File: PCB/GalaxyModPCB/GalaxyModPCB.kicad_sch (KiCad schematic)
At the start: 57 parts, among them J1 LED RGBW Connector, J2 USB to UART, J3 Motor Connector, J4 Projector Connector, J6 Power Header, J7 Boot mode, Q1 IRLML0030, Q2 IRLML0030, Q3 IRLML0030, Q4 IRLML0030, Q5 IRLML0030, Q6 IRLML0030, SW1 On/Off, SW2 Colour, SW3 Brightness, SW4 Motor, U1 ESP32-WROOM-32, U2 AMS1117-3.3

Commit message: Part separation for reconfiguration
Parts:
- J1: footprint Connector_JST:JST_PH_B5B-PH-K_1x05_P2.00mm_Vertical -> Connector_PinHeader_1.00mm:PinHeader_1x05_P1.00mm_Vertical
- J2: footprint Connector_JST:JST_PH_B3B-PH-K_1x03_P2.00mm_Vertical -> Connector_PinHeader_1.00mm:PinHeader_1x03_P1.00mm_Vertical
- J3, J4, J6, J7: footprint Connector_JST:JST_PH_B2B-PH-K_1x02_P2.00mm_Vertical -> Connector_PinHeader_1.00mm:PinHeader_1x02_P1.00mm_Vertical

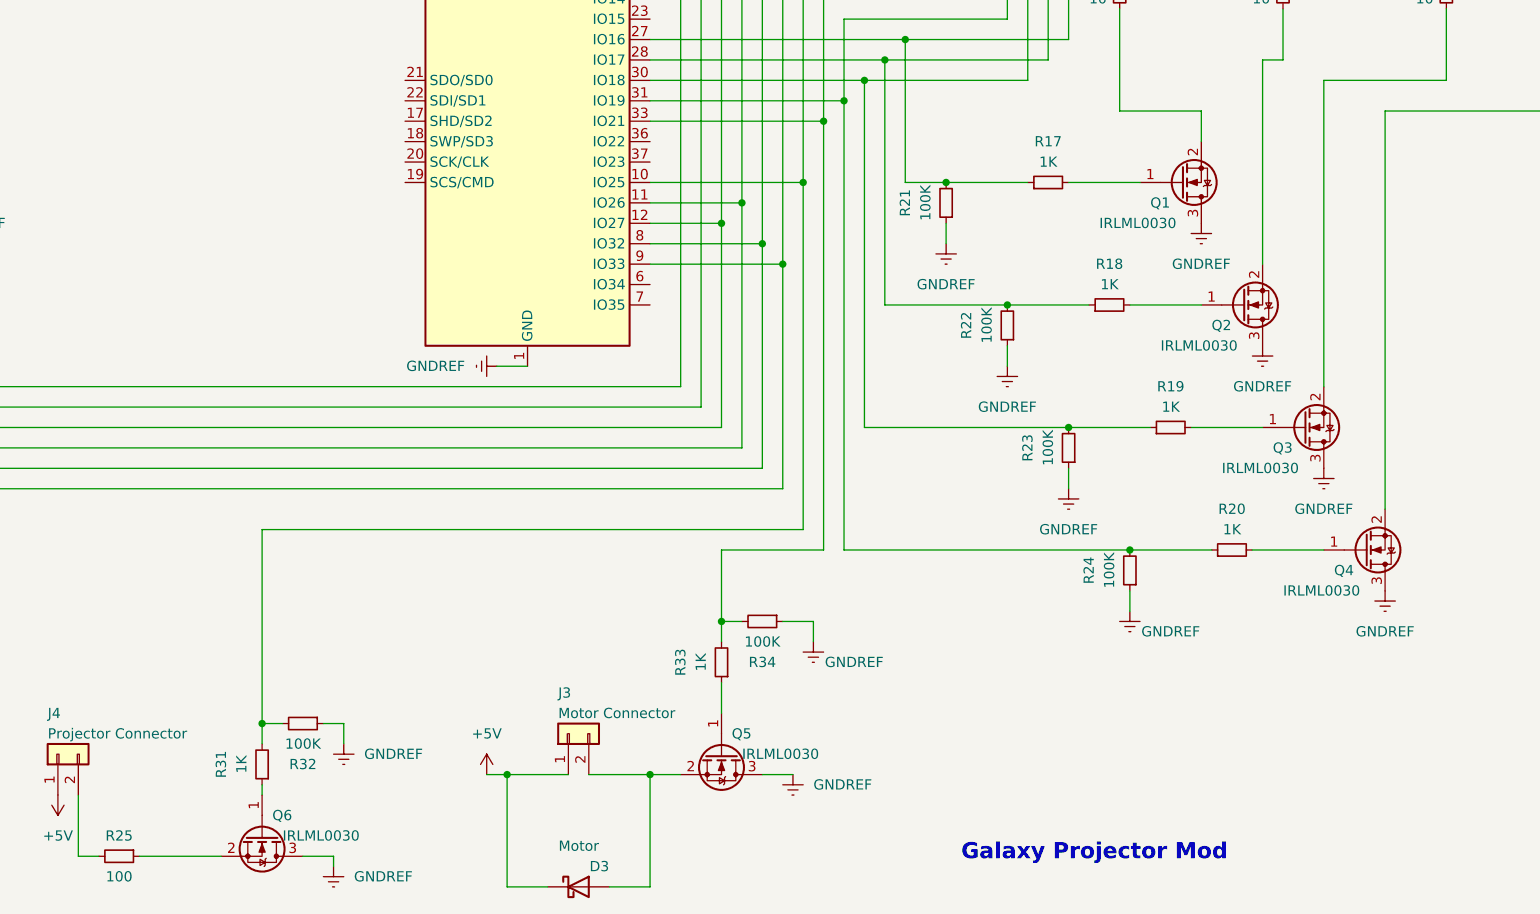
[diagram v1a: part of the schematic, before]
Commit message: Fixed transistor direction
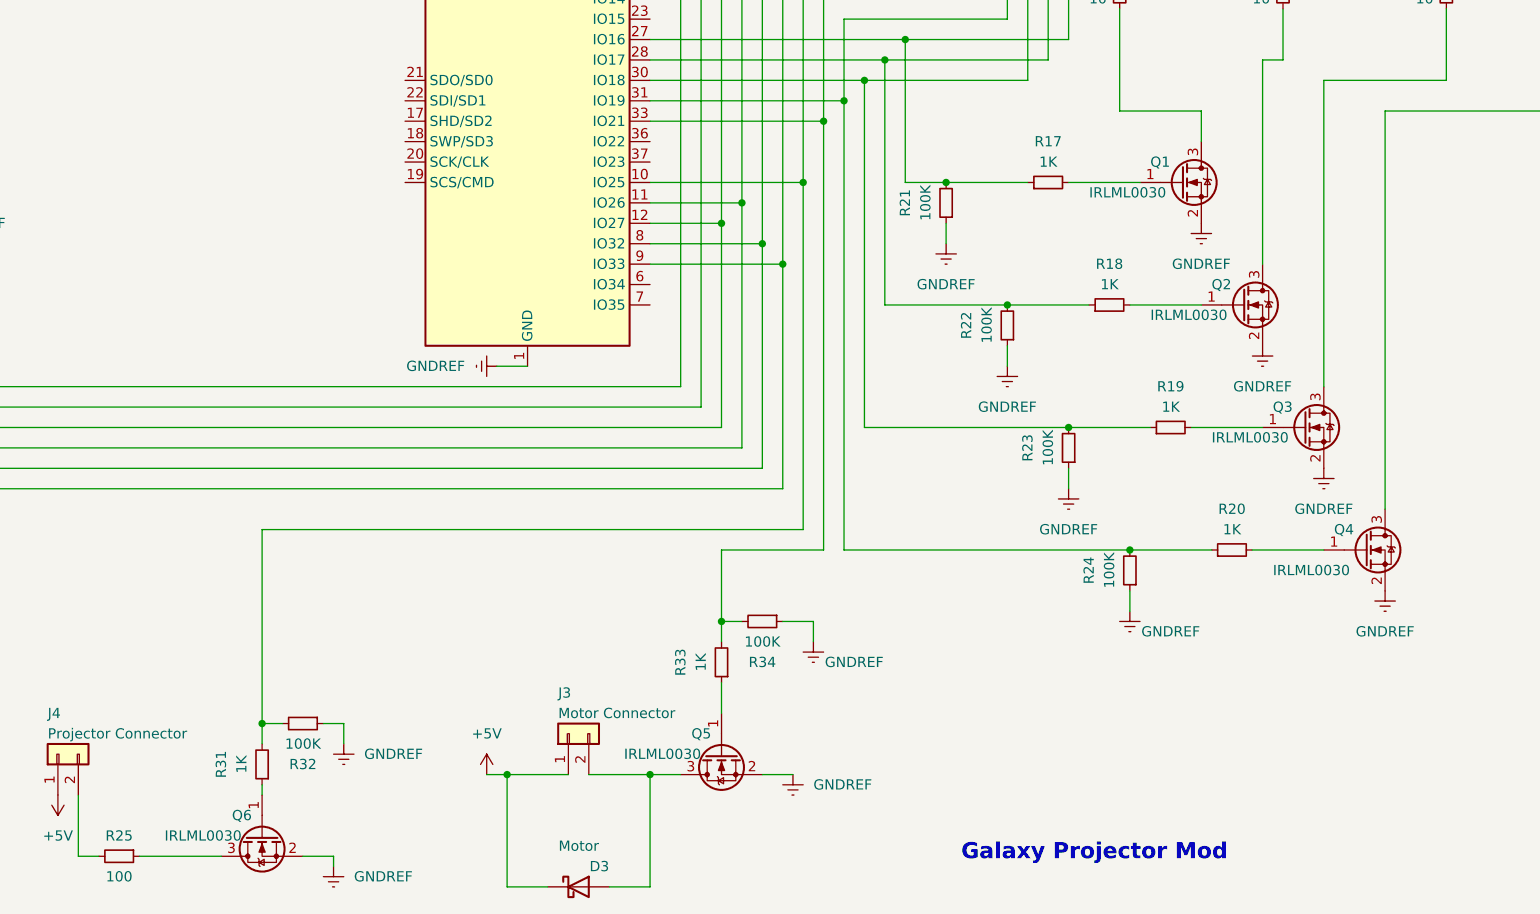
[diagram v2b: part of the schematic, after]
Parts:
- H1: footprint (none) -> MountingHole:MountingHole_2mm
- H3: footprint (none) -> MountingHole:MountingHole_2.5mm
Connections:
- net GNDREF: now also Q1.2 (S), Q2.2 (S), Q3.2 (S), Q4.2 (S), Q5.2 (S), Q6.2 (S); no longer Q1.3 (D), Q2.3 (D), Q3.3 (D), Q4.3 (D), Q5.3 (D), Q6.3 (D)
- net at R9.2: now also Q3.3 (D); no longer Q3.2 (S)
- net at R5.2: now also Q2.3 (D); no longer Q2.2 (S)
- net at D3.2 (A), J3.2 (Pin_2): now also Q5.3 (D); no longer Q5.2 (S)
- net at R1.2: now also Q1.3 (D); no longer Q1.2 (S)
- net at R13.2: now also Q4.3 (D); no longer Q4.2 (S)
- net at R25.1: now also Q6.3 (D); no longer Q6.2 (S)
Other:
- moved on the sheet: Q5, Q6
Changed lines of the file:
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@@
     (pin "1")
   )
-  (symbol (lib_id "Transistor_FET:IRLML0030") (at 220.98 121.92 0) (mirror x) (unit 1)
-    (in_bom yes) (on_board yes)
-    (property "Reference" "Q2" (id 0) (at 217.17 124.46 0)
-      (effects (font (size 1.27 1.27)) (justify left))
-    )
-    (property "Value" "IRLML0030" (id 1) (at 210.82 127 0)
-      (effects (font (size 1.27 1.27)) (justify left))
-    )
-    (property "Footprint" "Package_TO_SOT_SMD:SOT-23" (id 2) (at 226.06 120.015 0)
+  (symbol (lib_id "Transistor_FET:IRLML0030") (at 220.98 121.92 0) (unit 1)
+    (in_bom yes) (on_board yes)
+    (property "Reference" "Q2" (id 0) (at 217.17 119.38 0)
+      (effects (font (size 1.27 1.27)) (justify left))
+    )
+    (property "Value" "IRLML0030" (id 1) (at 209.55 123.19 0)
+      (effects (font (size 1.27 1.27)) (justify left))
+    )
+    (property "Footprint" "Package_TO_SOT_SMD:SOT-23" (id 2) (at 226.06 123.825 0)
       (effects (font (size 1.27 1.27) italic) (justify left) hide)
     )
@@
     (pin "1")
   )
-  (symbol (lib_id "Transistor_FET:IRLML0030") (at 156.21 177.8 270) (unit 1)
-    (in_bom yes) (on_board yes)
-    (property "Reference" "Q5" (id 0) (at 157.48 175.26 90)
-      (effects (font (size 1.27 1.27)) (justify left))
-    )
-    (property "Value" "IRLML0030" (id 1) (at 158.75 177.8 90)
-      (effects (font (size 1.27 1.27)) (justify left))
-    )
-    (property "Footprint" "Package_TO_SOT_SMD:SOT-23" (id 2) (at 154.305 182.88 0)
+  (symbol (lib_id "Transistor_FET:IRLML0030") (at 156.21 177.8 90) (mirror x) (unit 1)
+    (in_bom yes) (on_board yes)
+    (property "Reference" "Q5" (id 0) (at 154.94 175.26 90)
+      (effects (font (size 1.27 1.27)) (justify left))
+    )
+    (property "Value" "IRLML0030" (id 1) (at 153.67 177.8 90)
+      (effects (font (size 1.27 1.27)) (justify left))
+    )
+    (property "Footprint" "Package_TO_SOT_SMD:SOT-23" (id 2) (at 158.115 182.88 0)
       (effects (font (size 1.27 1.27) italic) (justify left) hide)
     )
@@
       (effects (font (size 1.27 1.27)) (justify left))
     )
-    (property "Footprint" "" (id 2) (at 36.83 80.01 0)
+    (property "Footprint" "MountingHole:MountingHole_2.5mm" (id 2) (at 36.83 80.01 0)
       (effects (font (size 1.27 1.27)) hide)
     )
@@
       (effects (font (size 1.27 1.27)) (justify left))
     )
-    (property "Footprint" "" (id 2) (at 36.83 73.66 0)
+    (property "Footprint" "MountingHole:MountingHole_2mm" (id 2) (at 36.83 73.66 0)
       (effects (font (size 1.27 1.27)) hide)
     )
@@
     (pin "1")
   )
-  (symbol (lib_id "Transistor_FET:IRLML0030") (at 213.36 106.68 0) (mirror x) (unit 1)
-    (in_bom yes) (on_board yes)
-    (property "Reference" "Q1" (id 0) (at 209.55 109.22 0)
-      (effects (font (size 1.27 1.27)) (justify left))
-    )
-    (property "Value" "IRLML0030" (id 1) (at 203.2 111.76 0)
-      (effects (font (size 1.27 1.27)) (justify left))
-    )
-    (property "Footprint" "Package_TO_SOT_SMD:SOT-23" (id 2) (at 218.44 104.775 0)
+  (symbol (lib_id "Transistor_FET:IRLML0030") (at 213.36 106.68 0) (unit 1)
+    (in_bom yes) (on_board yes)
+    (property "Reference" "Q1" (id 0) (at 209.55 104.14 0)
+      (effects (font (size 1.27 1.27)) (justify left))
+    )
+    (property "Value" "IRLML0030" (id 1) (at 201.93 107.95 0)
+      (effects (font (size 1.27 1.27)) (justify left))
+    )
+    (property "Footprint" "Package_TO_SOT_SMD:SOT-23" (id 2) (at 218.44 108.585 0)
       (effects (font (size 1.27 1.27) italic) (justify left) hide)
     )
@@
     (pin "2")
   )
-  (symbol (lib_id "Transistor_FET:IRLML0030") (at 228.6 137.16 0) (mirror x) (unit 1)
-    (in_bom yes) (on_board yes)
-    (property "Reference" "Q3" (id 0) (at 224.79 139.7 0)
-      (effects (font (size 1.27 1.27)) (justify left))
-    )
-    (property "Value" "IRLML0030" (id 1) (at 218.44 142.24 0)
-      (effects (font (size 1.27 1.27)) (justify left))
-    )
-    (property "Footprint" "Package_TO_SOT_SMD:SOT-23" (id 2) (at 233.68 135.255 0)
+  (symbol (lib_id "Transistor_FET:IRLML0030") (at 228.6 137.16 0) (unit 1)
+    (in_bom yes) (on_board yes)
+    (property "Reference" "Q3" (id 0) (at 224.79 134.62 0)
+      (effects (font (size 1.27 1.27)) (justify left))
+    )
+    (property "Value" "IRLML0030" (id 1) (at 217.17 138.43 0)
+      (effects (font (size 1.27 1.27)) (justify left))
+    )
+    (property "Footprint" "Package_TO_SOT_SMD:SOT-23" (id 2) (at 233.68 139.065 0)
       (effects (font (size 1.27 1.27) italic) (justify left) hide)
     )
@@
     (pin "3")
   )
-  (symbol (lib_id "Transistor_FET:IRLML0030") (at 236.22 152.4 0) (mirror x) (unit 1)
-    (in_bom yes) (on_board yes)
-    (property "Reference" "Q4" (id 0) (at 232.41 154.94 0)
-      (effects (font (size 1.27 1.27)) (justify left))
-    )
-    (property "Value" "IRLML0030" (id 1) (at 226.06 157.48 0)
-      (effects (font (size 1.27 1.27)) (justify left))
-    )
-    (property "Footprint" "Package_TO_SOT_SMD:SOT-23" (id 2) (at 241.3 150.495 0)
+  (symbol (lib_id "Transistor_FET:IRLML0030") (at 236.22 152.4 0) (unit 1)
+    (in_bom yes) (on_board yes)
+    (property "Reference" "Q4" (id 0) (at 232.41 149.86 0)
+      (effects (font (size 1.27 1.27)) (justify left))
+    )
+    (property "Value" "IRLML0030" (id 1) (at 224.79 154.94 0)
+      (effects (font (size 1.27 1.27)) (justify left))
+    )
+    (property "Footprint" "Package_TO_SOT_SMD:SOT-23" (id 2) (at 241.3 154.305 0)
       (effects (font (size 1.27 1.27) italic) (justify left) hide)
     )
@@
     (pin "2")
   )
-  (symbol (lib_id "Transistor_FET:IRLML0030") (at 99.06 187.96 270) (unit 1)
-    (in_bom yes) (on_board yes)
-    (property "Reference" "Q6" (id 0) (at 100.33 185.42 90)
-      (effects (font (size 1.27 1.27)) (justify left))
-    )
-    (property "Value" "IRLML0030" (id 1) (at 101.6 187.96 90)
-      (effects (font (size 1.27 1.27)) (justify left))
-    )
-    (property "Footprint" "Package_TO_SOT_SMD:SOT-23" (id 2) (at 97.155 193.04 0)
+  (symbol (lib_id "Transistor_FET:IRLML0030") (at 99.06 187.96 90) (mirror x) (unit 1)
+    (in_bom yes) (on_board yes)
+    (property "Reference" "Q6" (id 0) (at 97.79 185.42 90)
+      (effects (font (size 1.27 1.27)) (justify left))
+    )
+    (property "Value" "IRLML0030" (id 1) (at 96.52 187.96 90)
+      (effects (font (size 1.27 1.27)) (justify left))
+    )
+    (property "Footprint" "Package_TO_SOT_SMD:SOT-23" (id 2) (at 100.965 193.04 0)
       (effects (font (size 1.27 1.27) italic) (justify left) hide)
     )

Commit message: Updated diode footprints
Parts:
- D1, D3: footprint Diode_SMD:D_0805_2012Metric_Pad1.15x1.40mm_HandSolder -> Diode_SMD:D_SMA_Handsoldering
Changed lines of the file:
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@@
       (effects (font (size 1.27 1.27)) (justify right))
     )
-    (property "Footprint" "Diode_SMD:D_0805_2012Metric_Pad1.15x1.40mm_HandSolder" (id 2) (at 138.43 194.31 0)
+    (property "Footprint" "Diode_SMD:D_SMA_Handsoldering" (id 2) (at 138.43 194.31 0)
       (effects (font (size 1.27 1.27)) hide)
     )
@@
       (effects (font (size 1.27 1.27)) (justify right))
     )
-    (property "Footprint" "Diode_SMD:D_0805_2012Metric_Pad1.15x1.40mm_HandSolder" (id 2) (at 76.2 29.21 0)
+    (property "Footprint" "Diode_SMD:D_SMA_Handsoldering" (id 2) (at 76.2 29.21 0)
       (effects (font (size 1.27 1.27)) hide)
     )
@@
     )
     (path "/efc17c54-3240-40f4-ab40-6c297d686c7c"
-      (reference "D1") (unit 1) (value "RVP Diode") (footprint "Diode_SMD:D_0805_2012Metric_Pad1.15x1.40mm_HandSolder")
+      (reference "D1") (unit 1) (value "RVP Diode") (footprint "Diode_SMD:D_SMA_Handsoldering")
     )
     (path "/dd7f5c67-48b1-4411-b6b0-95c022f09402"
@@
     )
     (path "/b2da1734-3d24-417f-9434-39423f6151c2"
-      (reference "D3") (unit 1) (value "Motor") (footprint "Diode_SMD:D_0805_2012Metric_Pad1.15x1.40mm_HandSolder")
+      (reference "D3") (unit 1) (value "Motor") (footprint "Diode_SMD:D_SMA_Handsoldering")
     )
     (path "/9c814a5f-1e26-4b32-8e4a-3bff32939361"

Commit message: Updated annotations
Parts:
- added R3: 0, Resistor_SMD:R_0805_2012Metric_Pad1.20x1.40mm_HandSolder, symbol Device:R_Small
- renumbered C4 to C1, C9 to C2, C10 to C3, C2 to C4, C8 to C5, C7 to C6, C6 to C7, C5 to C8, J6 to J1, J7 to J2, J1 to J3, J2 to J4, J3 to J5, J4 to J6, R27 to R1, R21 to R10, R18 to R11, R22 to R12, R35 to R13, R19 to R14, R23 to R15, R36 to R16, R20 to R17, R24 to R18, R34 to R19, R30 to R2, R37 to R20, R33 to R21, R32 to R22, R31 to R23, R38 to R24, R39 to R4, R1 to R5, R5 to R6, R9 to R7, R13 to R8, R17 to R9, SW4 to SW1, SW3 to SW2, SW2 to SW3, SW1 to SW4, U2 to U1, U1 to U2
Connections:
- net +3.3V: no longer C2.1, C3.1, R4.2, U2.2 (VDD)
- net at R1.1, U1.2 (VO): now also R3.1
- new net: C2.1, C3.1, R3.2, R4.2, U2.2 (VDD)

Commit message: Rearranged componenets
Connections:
- net at C6.1, R16.2, SW2.1: now also U2.9 (IO33); no longer U2.11 (IO26)
- net at C5.1, R13.2, SW1.1: now also U2.8 (IO32); no longer U2.12 (IO27)
- net at C7.1, R20.2, SW3.1: now also U2.11 (IO26); no longer U2.8 (IO32)
- net at C8.1, R24.2, SW4.1: now also U2.12 (IO27); no longer U2.9 (IO33)
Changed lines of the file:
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@@
   (junction (at 78.74 29.21) (diameter 0) (color 0 0 0 0)
   )
-  (junction (at 158.75 109.22) (diameter 0) (color 0 0 0 0)
-  )
   (junction (at 173.99 93.98) (diameter 0) (color 0 0 0 0)
   )
@@
   (junction (at 40.64 160.02) (diameter 0) (color 0 0 0 0)
   )
+  (junction (at 161.29 109.22) (diameter 0) (color 0 0 0 0)
+  )
   (junction (at 166.37 106.68) (diameter 0) (color 0 0 0 0)
   )
@@
   (junction (at 199.39 137.16) (diameter 0) (color 0 0 0 0)
   )
-  (junction (at 161.29 114.3) (diameter 0) (color 0 0 0 0)
-  )
   (junction (at 99.06 38.1) (diameter 0) (color 0 0 0 0)
   )
   (junction (at 25.4 142.24) (diameter 0) (color 0 0 0 0)
   )
+  (junction (at 156.21 114.3) (diameter 0) (color 0 0 0 0)
+  )
   (junction (at 191.77 121.92) (diameter 0) (color 0 0 0 0)
   )
@@
   (junction (at 266.7 74.93) (diameter 0) (color 0 0 0 0)
   )
+  (junction (at 158.75 116.84) (diameter 0) (color 0 0 0 0)
+  )
   (junction (at 115.57 63.5) (diameter 0) (color 0 0 0 0)
   )
   (junction (at 176.53 91.44) (diameter 0) (color 0 0 0 0)
   )
+  (junction (at 163.83 111.76) (diameter 0) (color 0 0 0 0)
+  )
   (junction (at 25.4 177.8) (diameter 0) (color 0 0 0 0)
   )
-  (junction (at 163.83 116.84) (diameter 0) (color 0 0 0 0)
-  )
   (junction (at 132.08 49.53) (diameter 0) (color 0 0 0 0)
   )
@@
   (junction (at 179.07 88.9) (diameter 0) (color 0 0 0 0)
   )
-  (junction (at 156.21 111.76) (diameter 0) (color 0 0 0 0)
-  )
   (junction (at 220.98 67.31) (diameter 0) (color 0 0 0 0)
   )
@@
     (stroke (width 0) (type default) (color 0 0 0 0))
   )
+  (wire (pts (xy 156.21 114.3) (xy 156.21 137.16))
+    (stroke (width 0) (type default) (color 0 0 0 0))
+  )
   (wire (pts (xy 184.15 78.74) (xy 184.15 50.8))
     (stroke (width 0) (type default) (color 0 0 0 0))
@@
     (stroke (width 0) (type default) (color 0 0 0 0))
   )
-  (wire (pts (xy 147.32 109.22) (xy 158.75 109.22))
-    (stroke (width 0) (type default) (color 0 0 0 0))
-  )
   (wire (pts (xy 76.2 24.13) (xy 76.2 25.4))
     (stroke (width 0) (type default) (color 0 0 0 0))
@@
     (stroke (width 0) (type default) (color 0 0 0 0))
   )
+  (wire (pts (xy 158.75 116.84) (xy 158.75 139.7))
+    (stroke (width 0) (type default) (color 0 0 0 0))
+  )
   (wire (pts (xy 76.2 38.1) (xy 83.82 38.1))
     (stroke (width 0) (type default) (color 0 0 0 0))
@@
     (stroke (width 0) (type default) (color 0 0 0 0))
   )
+  (wire (pts (xy 147.32 111.76) (xy 163.83 111.76))
+    (stroke (width 0) (type default) (color 0 0 0 0))
+  )
   (wire (pts (xy 46.99 124.46) (xy 46.99 125.73))
     (stroke (width 0) (type default) (color 0 0 0 0))
@@
     (stroke (width 0) (type default) (color 0 0 0 0))
   )
+  (wire (pts (xy 147.32 114.3) (xy 156.21 114.3))
+    (stroke (width 0) (type default) (color 0 0 0 0))
+  )
   (wire (pts (xy 25.4 184.15) (xy 25.4 177.8))
     (stroke (width 0) (type default) (color 0 0 0 0))
@@
     (stroke (width 0) (type default) (color 0 0 0 0))
   )
-  (wire (pts (xy 161.29 76.2) (xy 161.29 114.3))
-    (stroke (width 0) (type default) (color 0 0 0 0))
-  )
   (wire (pts (xy 38.1 160.02) (xy 40.64 160.02))
     (stroke (width 0) (type default) (color 0 0 0 0))
@@
     (stroke (width 0) (type default) (color 0 0 0 0))
   )
-  (wire (pts (xy 147.32 111.76) (xy 156.21 111.76))
-    (stroke (width 0) (type default) (color 0 0 0 0))
-  )
   (wire (pts (xy 207.01 152.4) (xy 217.17 152.4))
     (stroke (width 0) (type default) (color 0 0 0 0))
@@
     (stroke (width 0) (type default) (color 0 0 0 0))
   )
+  (wire (pts (xy 147.32 109.22) (xy 161.29 109.22))
+    (stroke (width 0) (type default) (color 0 0 0 0))
+  )
   (wire (pts (xy 166.37 106.68) (xy 166.37 149.86))
     (stroke (width 0) (type default) (color 0 0 0 0))
@@
     (stroke (width 0) (type default) (color 0 0 0 0))
   )
-  (wire (pts (xy 147.32 114.3) (xy 161.29 114.3))
-    (stroke (width 0) (type default) (color 0 0 0 0))
-  )
   (wire (pts (xy 204.47 50.8) (xy 204.47 72.39))
     (stroke (width 0) (type default) (color 0 0 0 0))
@@
     (stroke (width 0) (type default) (color 0 0 0 0))
   )
-  (wire (pts (xy 158.75 73.66) (xy 158.75 109.22))
-    (stroke (width 0) (type default) (color 0 0 0 0))
-  )
   (wire (pts (xy 29.21 130.81) (xy 25.4 130.81))
     (stroke (width 0) (type default) (color 0 0 0 0))
@@
     (stroke (width 0) (type default) (color 0 0 0 0))
   )
-  (wire (pts (xy 147.32 116.84) (xy 163.83 116.84))
-    (stroke (width 0) (type default) (color 0 0 0 0))
-  )
   (wire (pts (xy 194.31 93.98) (xy 194.31 50.8))
     (stroke (width 0) (type default) (color 0 0 0 0))
@@
     (stroke (width 0) (type default) (color 0 0 0 0))
   )
-  (wire (pts (xy 158.75 109.22) (xy 158.75 139.7))
+  (wire (pts (xy 158.75 73.66) (xy 158.75 116.84))
     (stroke (width 0) (type default) (color 0 0 0 0))
   )
@@
     (stroke (width 0) (type default) (color 0 0 0 0))
   )
+  (wire (pts (xy 147.32 116.84) (xy 158.75 116.84))
+    (stroke (width 0) (type default) (color 0 0 0 0))
+  )
   (wire (pts (xy 25.4 160.02) (xy 27.94 160.02))
     (stroke (width 0) (type default) (color 0 0 0 0))
@@
     (stroke (width 0) (type default) (color 0 0 0 0))
   )
+  (wire (pts (xy 163.83 111.76) (xy 163.83 144.78))
+    (stroke (width 0) (type default) (color 0 0 0 0))
+  )
   (wire (pts (xy 99.06 176.53) (xy 99.06 173.99))
     (stroke (width 0) (type default) (color 0 0 0 0))
@@
     (stroke (width 0) (type default) (color 0 0 0 0))
   )
-  (wire (pts (xy 161.29 114.3) (xy 161.29 142.24))
+  (wire (pts (xy 161.29 76.2) (xy 161.29 109.22))
     (stroke (width 0) (type default) (color 0 0 0 0))
   )
@@
     (stroke (width 0) (type default) (color 0 0 0 0))
   )
-  (wire (pts (xy 156.21 71.12) (xy 156.21 111.76))
-    (stroke (width 0) (type default) (color 0 0 0 0))
-  )
   (wire (pts (xy 46.99 166.37) (xy 46.99 167.64))
     (stroke (width 0) (type default) (color 0 0 0 0))
@@
     (stroke (width 0) (type default) (color 0 0 0 0))
   )
-  (wire (pts (xy 163.83 78.74) (xy 163.83 116.84))
-    (stroke (width 0) (type default) (color 0 0 0 0))
-  )
   (wire (pts (xy 151.13 71.12) (xy 151.13 132.08))
     (stroke (width 0) (type default) (color 0 0 0 0))
@@
     (stroke (width 0) (type default) (color 0 0 0 0))
   )
+  (wire (pts (xy 161.29 109.22) (xy 161.29 142.24))
+    (stroke (width 0) (type default) (color 0 0 0 0))
+  )
   (wire (pts (xy 25.4 130.81) (xy 25.4 124.46))
     (stroke (width 0) (type default) (color 0 0 0 0))
@@
     (stroke (width 0) (type default) (color 0 0 0 0))
   )
-  (wire (pts (xy 163.83 116.84) (xy 163.83 144.78))
+  (wire (pts (xy 163.83 78.74) (xy 163.83 111.76))
     (stroke (width 0) (type default) (color 0 0 0 0))
   )
@@
     (stroke (width 0) (type default) (color 0 0 0 0))
   )
-  (wire (pts (xy 156.21 111.76) (xy 156.21 137.16))
-    (stroke (width 0) (type default) (color 0 0 0 0))
-  )
+  (wire (pts (xy 156.21 71.12) (xy 156.21 114.3))
+    (stroke (width 0) (type default) (color 0 0 0 0))
+  )
